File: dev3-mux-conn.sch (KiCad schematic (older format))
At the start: 8 parts, among them J29 Device 3, U11 MAX4533, U14 74LS32, U39 LTC1391, U40 LTC1391, U41 LTC1391, U7 TS12A44514

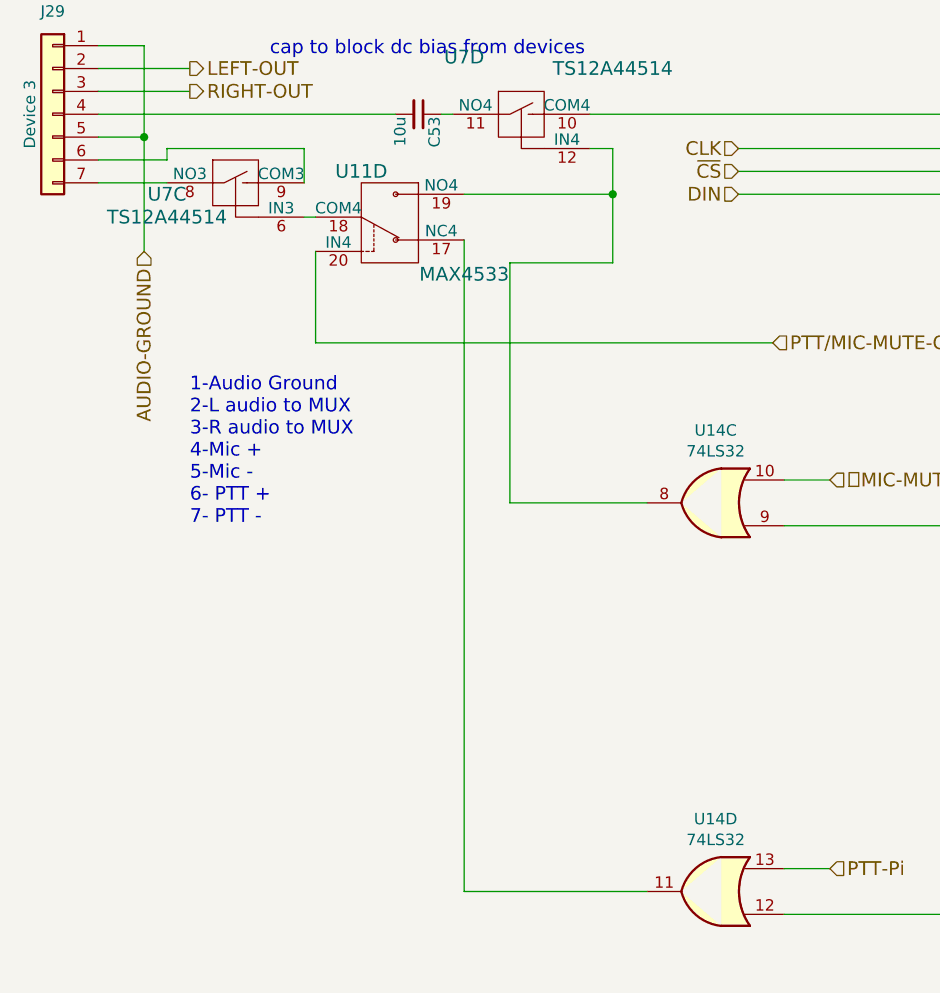
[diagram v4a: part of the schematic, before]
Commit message: Re arranging pins and component names
to make pcb layout saner
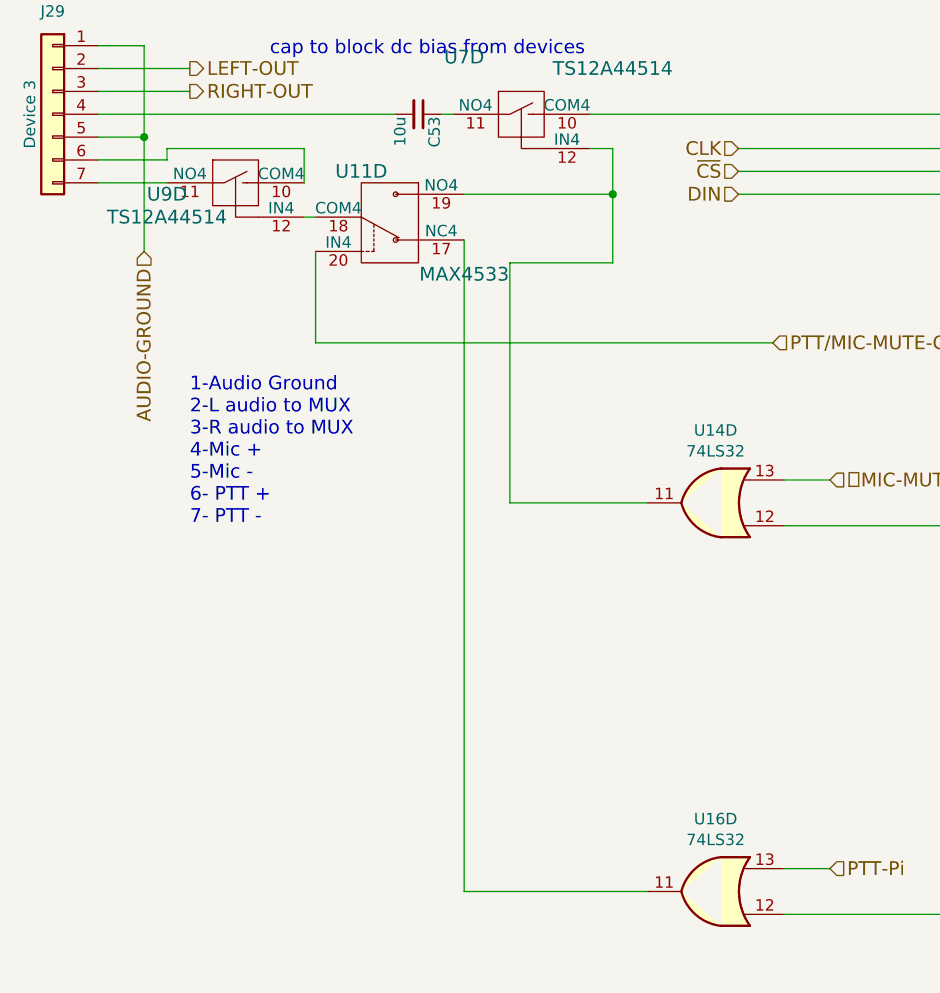
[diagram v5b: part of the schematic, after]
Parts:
- U14: Pricing (none) -> 0.00@0
- U16: renamed from U14; Pricing (none) -> 0.00@0
- renumbered U7 to U9
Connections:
- net MIC-MUTE-Pi: now also U14.13; no longer U14.10
- net at J29.6 (Pin_6): now also U9.10 (COM4); no longer U9.9 (COM3)
- net at J29.7 (Pin_7): now also U9.11 (NO4); no longer U9.8 (NO3)
- net at U11.19 (NO4), U7.12 (IN4): now also U14.11; no longer U14.8
- net at U11.18 (COM4): now also U9.12 (IN4); no longer U9.6 (IN3)
- net at U40.15 (D): now also U14.12; no longer U14.9
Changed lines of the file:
@@
 $Comp
 L TS12A44514 U?
-U 3 1 58EAAC3F
+U 4 1 58EAAC3F
 P 1650 1500
 AR Path="/58DEDA38/58EAAC3F" Ref="U?"  Part="1"
 AR Path="/58DEDA38/58E9E25B/58EAAC3F" Ref="U?"  Part="1"
-AR Path="/58DEDA38/58E9E9F4/58EAAC3F" Ref="U7"  Part="3"
-F 0 "U7" H 1350 1450 60  0000 C CNN
+AR Path="/58DEDA38/58E9E9F4/58EAAC3F" Ref="U9"  Part="4"
+F 0 "U9" H 1350 1450 60  0000 C CNN
 F 1 "TS12A44514" H 1350 1350 60  0000 C CNN
 F 2 "Housings_SSOP:TSSOP-14_4.4x5mm_Pitch0.65mm" H 2150 2800 60  0001 C CNN
@@
 F 7 "TSSOP14" H 1950 2700 60  0001 C CNN "Package ID"
 F 8 "0.00@0" H 1700 2500 60  0001 C CNN "Pricing"
-	3    1650 1500
+	4    1650 1500
 	1    0    0    -1
 $EndComp
@@
 $Comp
 L 74LS32 U?
-U 3 1 59D24359
+U 4 1 59D24359
 P 3750 2900
 AR Path="/58DEDA38/58E9E2BE/59D24359" Ref="U?"  Part="1"
-AR Path="/58DEDA38/58E9E9F4/59D24359" Ref="U14"  Part="3"
+AR Path="/58DEDA38/58E9E9F4/59D24359" Ref="U14"  Part="4"
 F 0 "U14" H 3750 2583 50  0000 C CNN
 F 1 "74LS32" H 3750 2674 50  0000 C CNN
 F 2 "Housings_SSOP:SSOP-14_5.3x6.2mm_Pitch0.65mm" H 3750 2900 50  0001 C CNN
 F 3 "" H 3750 2900 50  0001 C CNN
-	3    3750 2900
+F 4 "0.00@0" H 3750 2900 60  0001 C CNN "Pricing"
+	4    3750 2900
 	-1   0    0    1
 $EndComp
@@
 P 3750 4600
 AR Path="/58DEDA38/58E9E2BE/59D24361" Ref="U?"  Part="2"
-AR Path="/58DEDA38/58E9E9F4/59D24361" Ref="U14"  Part="4"
-F 0 "U14" H 3750 4283 50  0000 C CNN
+AR Path="/58DEDA38/58E9E9F4/59D24361" Ref="U16"  Part="4"
+F 0 "U16" H 3750 4283 50  0000 C CNN
 F 1 "74LS32" H 3750 4374 50  0000 C CNN
 F 2 "Housings_SSOP:SSOP-14_5.3x6.2mm_Pitch0.65mm" H 3750 4600 50  0001 C CNN
 F 3 "" H 3750 4600 50  0001 C CNN
+F 4 "0.00@0" H 3750 4600 60  0001 C CNN "Pricing"
 	4    3750 4600
 	-1   0    0    1

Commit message: Adding libraries and Notes
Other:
- note added: "Device power provided by\nexternal connection"
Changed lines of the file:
@@
 LIBS:interface
 LIBS:SW-gElectroMech
+LIBS:SW-Analog
+LIBS:SW-Semtech
 LIBS:edc-mux-board-cache
 EELAYER 26 0
@@
 	1    0    0    -1
 $EndComp
+Text Notes -550 1200 0    60   ~ 0
+Device power provided by\nexternal connection
 $EndSCHEMATC
